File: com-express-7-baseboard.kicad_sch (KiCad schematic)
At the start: 0 parts

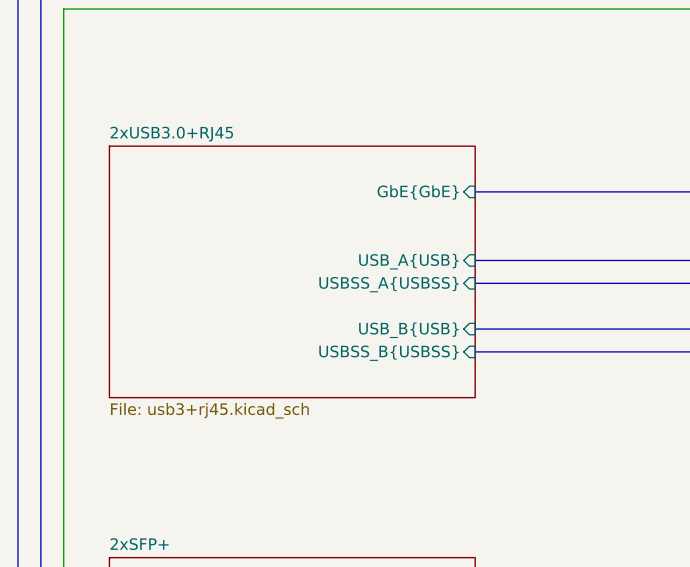
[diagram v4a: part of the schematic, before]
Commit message: [#57056] Connect USB 3.0 connectors on combo connector
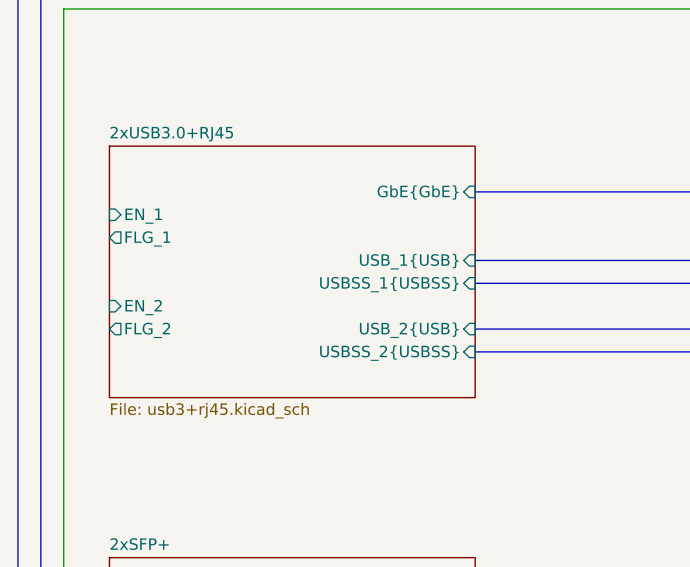
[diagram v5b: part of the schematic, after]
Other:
- sheet 2xUSB3.0+RJ45 ports: added EN_1, EN_2, FLG_1, FLG_2, USBSS_1{USBSS}, USBSS_2{USBSS}, USB_1{USB}, USB_2{USB}; removed USBSS_A{USBSS}, USBSS_B{USBSS}, USB_A{USB}, USB_B{USB}
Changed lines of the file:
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@@
       (effects (font (size 1.27 1.27)) (justify right))
     )
-    (pin "USBSS_A{USBSS}" input (at 137.16 73.66 0)
+    (pin "EN_1" input (at 96.52 66.04 180)
+      (effects (font (size 1.27 1.27)) (justify left))
+    )
+    (pin "FLG_1" output (at 96.52 68.58 180)
+      (effects (font (size 1.27 1.27)) (justify left))
+    )
+    (pin "USB_1{USB}" input (at 137.16 71.12 0)
       (effects (font (size 1.27 1.27)) (justify right))
     )
-    (pin "USBSS_B{USBSS}" input (at 137.16 81.28 0)
+    (pin "USBSS_1{USBSS}" input (at 137.16 73.66 0)
       (effects (font (size 1.27 1.27)) (justify right))
     )
-    (pin "USB_A{USB}" input (at 137.16 71.12 0)
+    (pin "USB_2{USB}" input (at 137.16 78.74 0)
       (effects (font (size 1.27 1.27)) (justify right))
     )
-    (pin "USB_B{USB}" input (at 137.16 78.74 0)
+    (pin "USBSS_2{USBSS}" input (at 137.16 81.28 0)
       (effects (font (size 1.27 1.27)) (justify right))
     )
+    (pin "EN_2" input (at 96.52 76.2 180)
+      (effects (font (size 1.27 1.27)) (justify left))
+    )
+    (pin "FLG_2" output (at 96.52 78.74 180)
+      (effects (font (size 1.27 1.27)) (justify left))
+    )
     (instances

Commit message: [#57056] Connect GbE
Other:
- sheet 2xUSB3.0+RJ45 ports: added ~{GBE0_ACT}, ~{GBE0_LINK_1000}, ~{GBE0_LINK_100}; removed none
- sheet Com Express 7 Interfaces ports: added ~{GBE0_ACT}, ~{GBE0_LINK_1000}, ~{GBE0_LINK_100}; removed none
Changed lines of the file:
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@@
     (stroke (width 0) (type default) (color 0 0 255 1))
   )
-  (bus (pts (xy 137.16 73.66) (xy 162.56 73.66))
+  (bus (pts (xy 137.16 81.28) (xy 162.56 81.28))
     (stroke (width 0) (type default) (color 0 255 255 1))
   )
@@
     (stroke (width 0) (type default) (color 255 0 0 1))
   )
+  (wire (pts (xy 137.16 73.66) (xy 162.56 73.66))
+    (stroke (width 0) (type default))
+  )
   (bus (pts (xy 96.52 152.4) (xy 86.36 152.4))
     (stroke (width 0) (type default))
@@
     (stroke (width 0) (type default))
   )
-  (bus (pts (xy 137.16 71.12) (xy 162.56 71.12))
+  (bus (pts (xy 137.16 78.74) (xy 162.56 78.74))
     (stroke (width 0) (type default) (color 0 0 255 1))
   )
@@
     (stroke (width 0) (type default))
   )
-  (bus (pts (xy 137.16 78.74) (xy 162.56 78.74))
+  (bus (pts (xy 137.16 86.36) (xy 162.56 86.36))
     (stroke (width 0) (type default) (color 0 0 255 1))
   )
@@
     (stroke (width 0) (type default))
   )
-  (bus (pts (xy 137.16 81.28) (xy 162.56 81.28))
+  (bus (pts (xy 137.16 88.9) (xy 162.56 88.9))
     (stroke (width 0) (type default) (color 0 255 255 1))
   )
@@
     (stroke (width 0) (type default))
   )
+  (wire (pts (xy 137.16 68.58) (xy 162.56 68.58))
+    (stroke (width 0) (type default))
+  )
   (bus (pts (xy 248.92 180.34) (xy 259.08 180.34))
     (stroke (width 0) (type default) (color 255 153 0 1))
@@
     (stroke (width 0) (type default))
   )
+  (wire (pts (xy 137.16 71.12) (xy 162.56 71.12))
+    (stroke (width 0) (type default))
+  )
   (wire (pts (xy 325.12 66.04) (xy 325.12 35.56))
     (stroke (width 0) (type default))
@@
       (effects (font (size 1.27 1.27)) (justify right))
     )
-    (pin "USB3{USB}" output (at 162.56 78.74 180)
-      (effects (font (size 1.27 1.27)) (justify left))
-    )
-    (pin "USB2{USB}" output (at 162.56 71.12 180)
+    (pin "USB3{USB}" output (at 162.56 86.36 180)
+      (effects (font (size 1.27 1.27)) (justify left))
+    )
+    (pin "USB2{USB}" output (at 162.56 78.74 180)
       (effects (font (size 1.27 1.27)) (justify left))
     )
@@
       (effects (font (size 1.27 1.27)) (justify right))
     )
-    (pin "USBSS3{USBSS}" output (at 162.56 81.28 180)
-      (effects (font (size 1.27 1.27)) (justify left))
-    )
-    (pin "USBSS2{USBSS}" output (at 162.56 73.66 180)
+    (pin "USBSS3{USBSS}" output (at 162.56 88.9 180)
+      (effects (font (size 1.27 1.27)) (justify left))
+    )
+    (pin "USBSS2{USBSS}" output (at 162.56 81.28 180)
       (effects (font (size 1.27 1.27)) (justify left))
     )
@@
       (effects (font (size 1.27 1.27)) (justify right))
     )
+    (pin "~{GBE0_ACT}" output (at 162.56 73.66 180)
+      (effects (font (size 1.27 1.27)) (justify left))
+    )
+    (pin "~{GBE0_LINK_1000}" output (at 162.56 68.58 180)
+      (effects (font (size 1.27 1.27)) (justify left))
+    )
+    (pin "~{GBE0_LINK_100}" output (at 162.56 71.12 180)
+      (effects (font (size 1.27 1.27)) (justify left))
+    )
     (instances
       (project "com-express-7-baseboard"
@@
     )
   )
-  (sheet (at 96.52 58.42) (size 40.64 27.94) (fields_autoplaced)
+  (sheet (at 96.52 58.42) (size 40.64 33.02) (fields_autoplaced)
     (stroke (width 0.1524) (type solid))
     (fill (color 0 0 0 0.0000))
@@
       (effects (font (size 1.27 1.27)) (justify left bottom))
     )
-    (property "Sheetfile" "usb3+rj45.kicad_sch" (at 96.52 86.9446 0)
+    (property "Sheetfile" "usb3+rj45.kicad_sch" (at 96.52 92.0246 0)
       (effects (font (size 1.27 1.27)) (justify left top))
     )
@@
       (effects (font (size 1.27 1.27)) (justify left))
     )
-    (pin "USB_1{USB}" input (at 137.16 71.12 0)
-      (effects (font (size 1.27 1.27)) (justify right))
-    )
-    (pin "USBSS_1{USBSS}" input (at 137.16 73.66 0)
-      (effects (font (size 1.27 1.27)) (justify right))
-    )
-    (pin "USB_2{USB}" input (at 137.16 78.74 0)
-      (effects (font (size 1.27 1.27)) (justify right))
-    )
-    (pin "USBSS_2{USBSS}" input (at 137.16 81.28 0)
+    (pin "USB_1{USB}" input (at 137.16 78.74 0)
+      (effects (font (size 1.27 1.27)) (justify right))
+    )
+    (pin "USBSS_1{USBSS}" input (at 137.16 81.28 0)
+      (effects (font (size 1.27 1.27)) (justify right))
+    )
+    (pin "USB_2{USB}" input (at 137.16 86.36 0)
+      (effects (font (size 1.27 1.27)) (justify right))
+    )
+    (pin "USBSS_2{USBSS}" input (at 137.16 88.9 0)
       (effects (font (size 1.27 1.27)) (justify right))
     )
@@
       (effects (font (size 1.27 1.27)) (justify left))
     )
-    (instances
+    (pin "~{GBE0_LINK_1000}" input (at 137.16 68.58 0)
+      (effects (font (size 1.27 1.27)) (justify right))
+    )
+    (pin "~{GBE0_ACT}" input (at 137.16 73.66 0)
+      (effects (font (size 1.27 1.27)) (justify right))
+    )
+    (pin "~{GBE0_LINK_100}" input (at 137.16 71.12 0)
+      (effects (font (size 1.27 1.27)) (justify right))
+    )
+    (instances

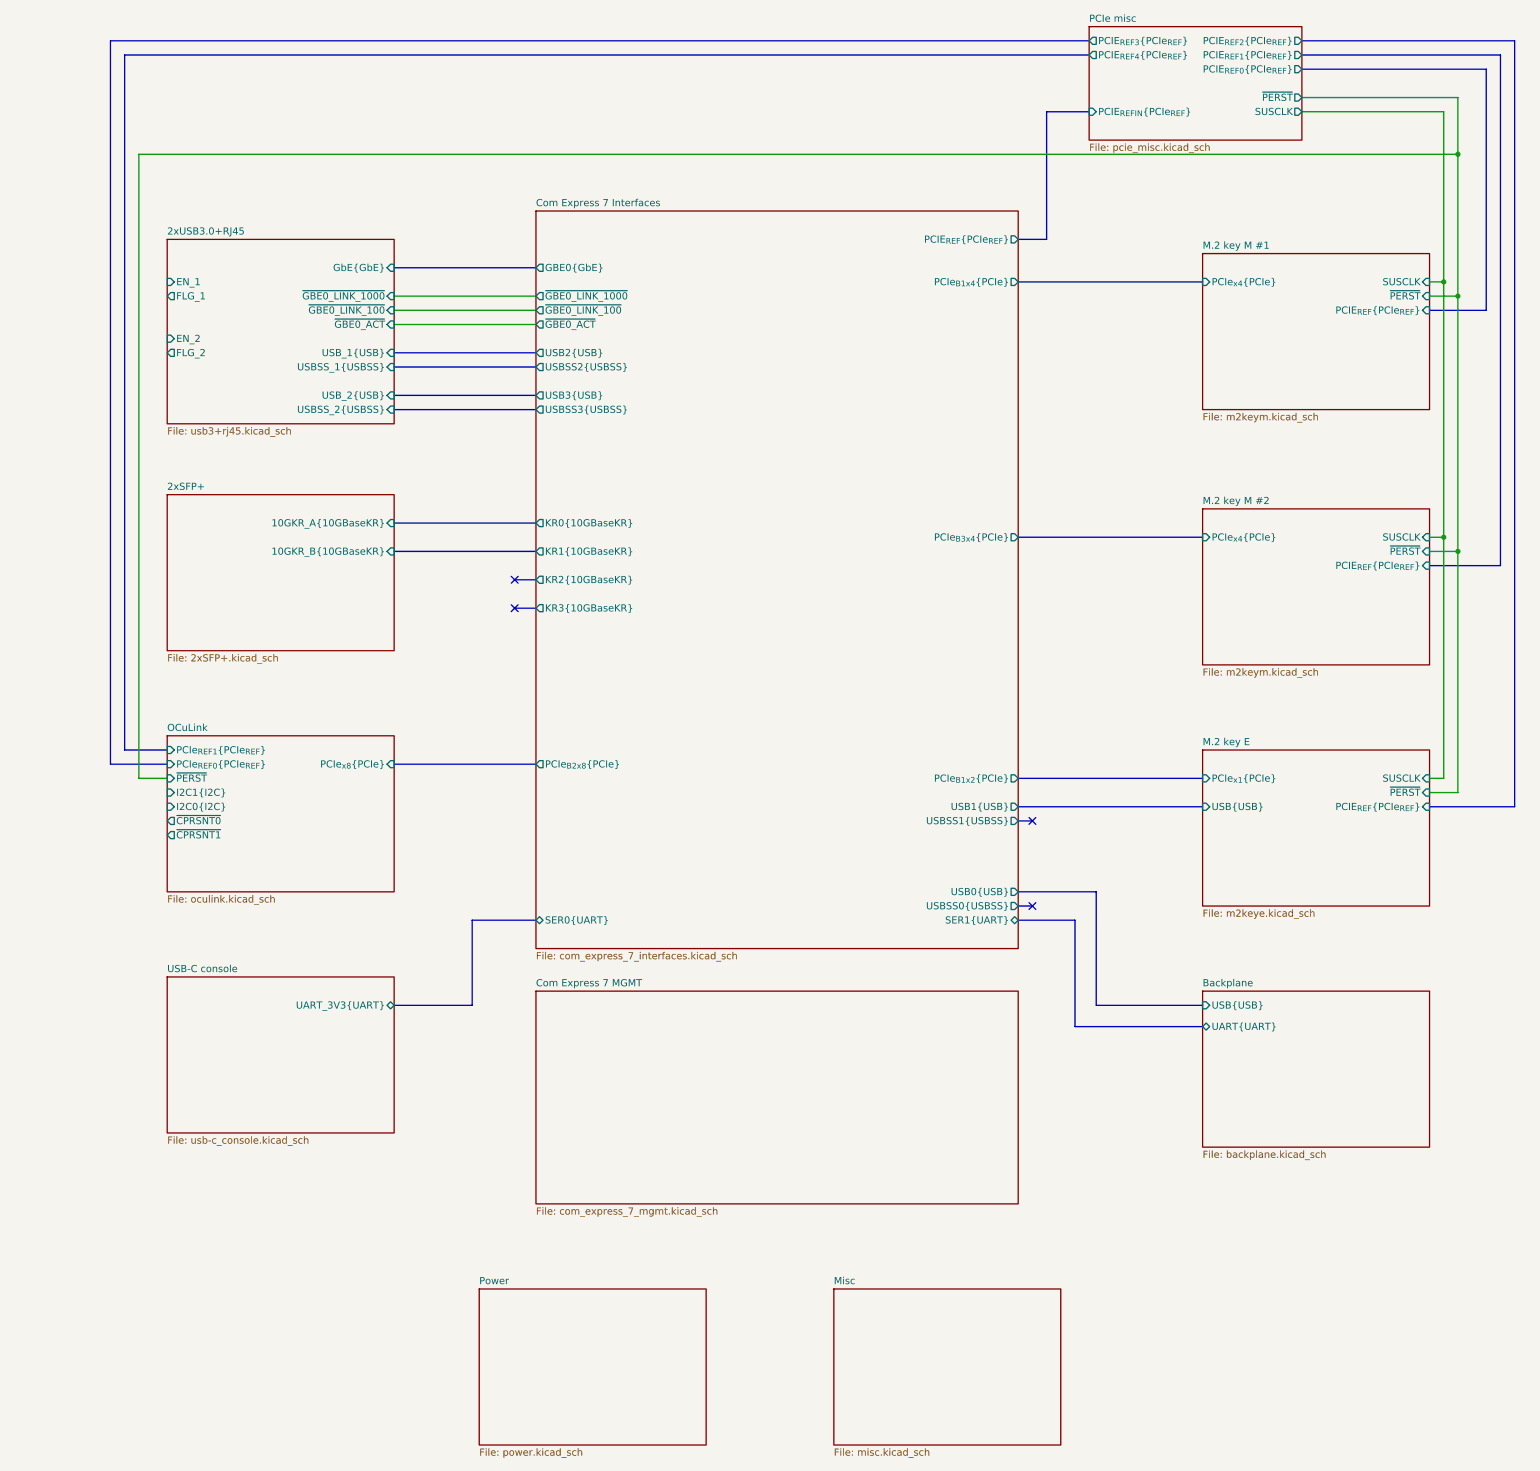
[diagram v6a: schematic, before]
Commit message: [#57056] Update top sheet, update sheet's dates
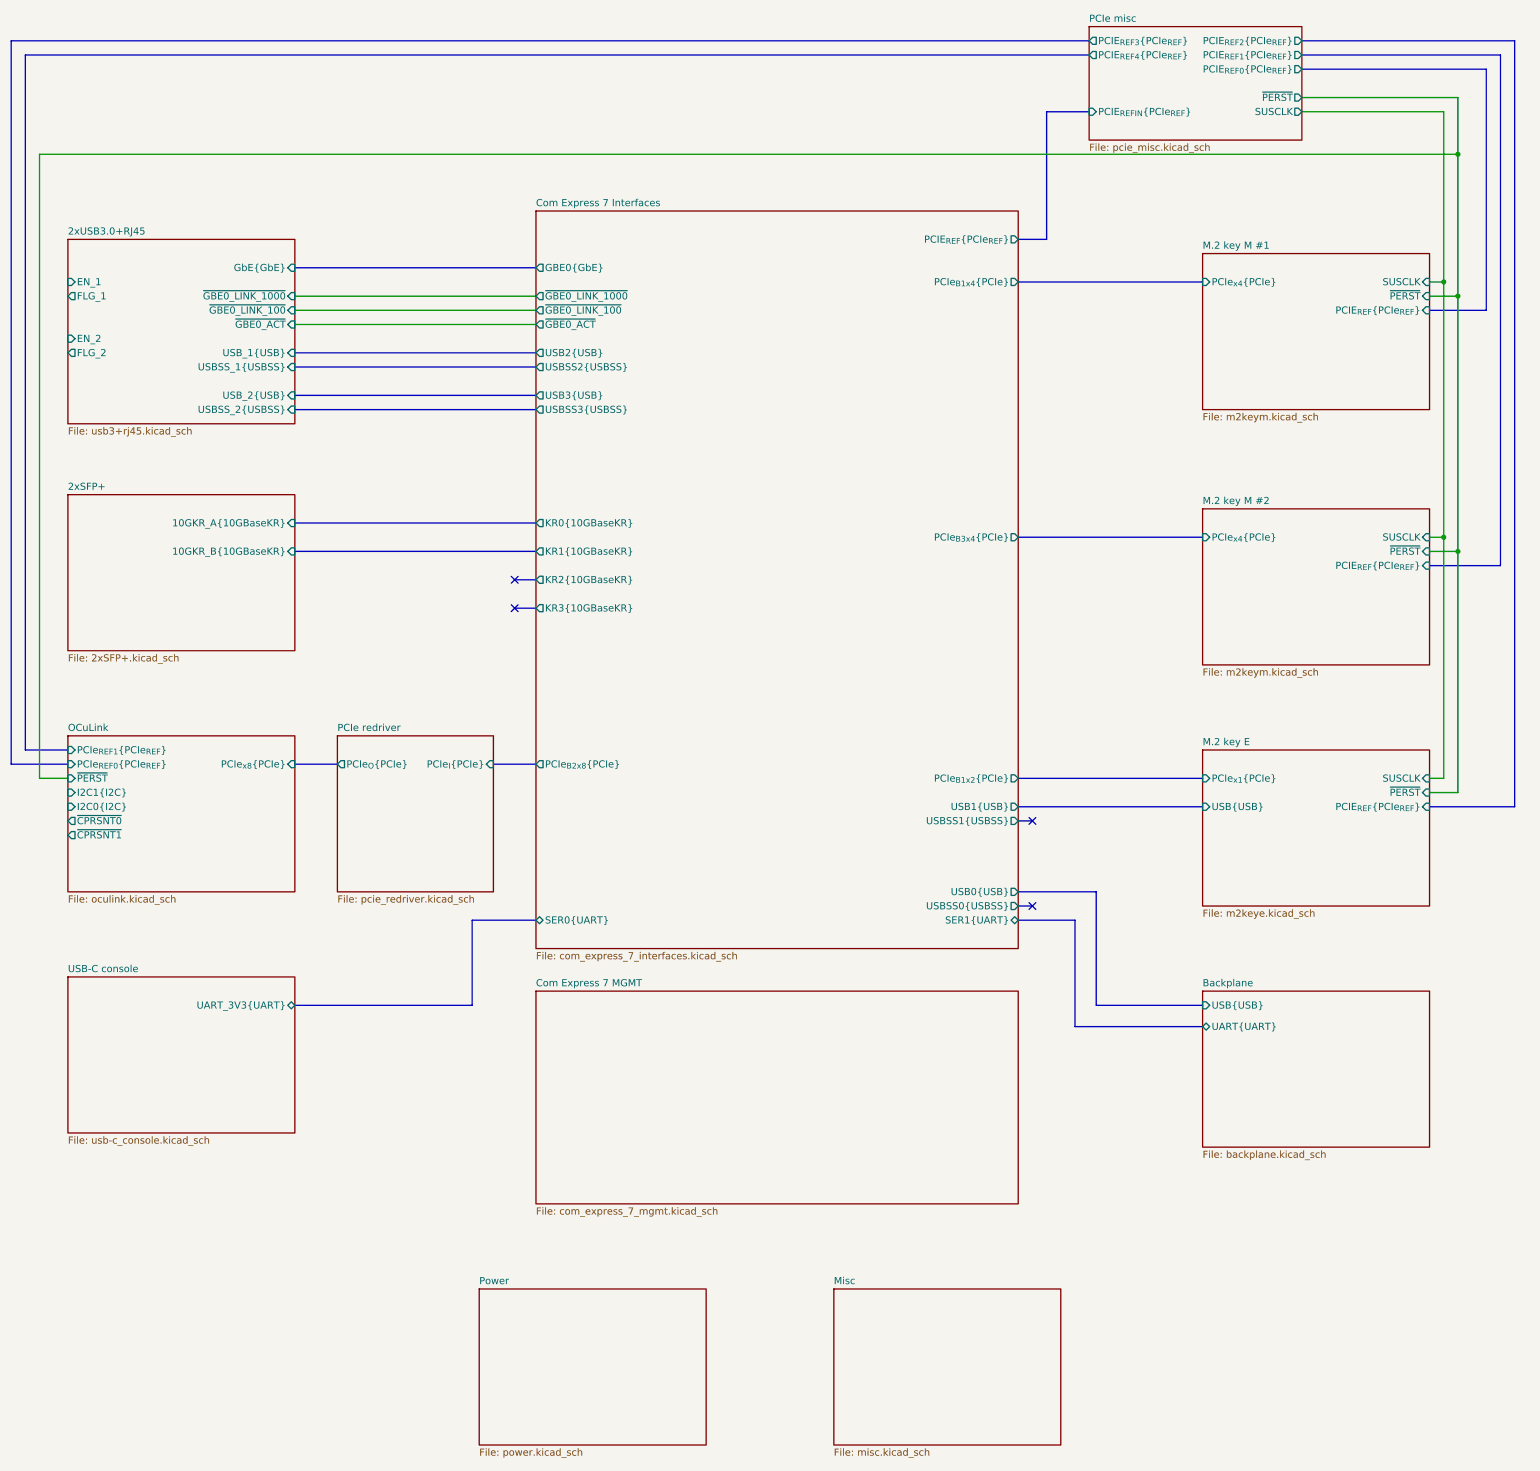
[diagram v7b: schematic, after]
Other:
- added sheet PCIe redriver (pcie_redriver.kicad_sch)

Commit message: [#57056] Update PCIe lane assignment, drop 2nd OCuLink
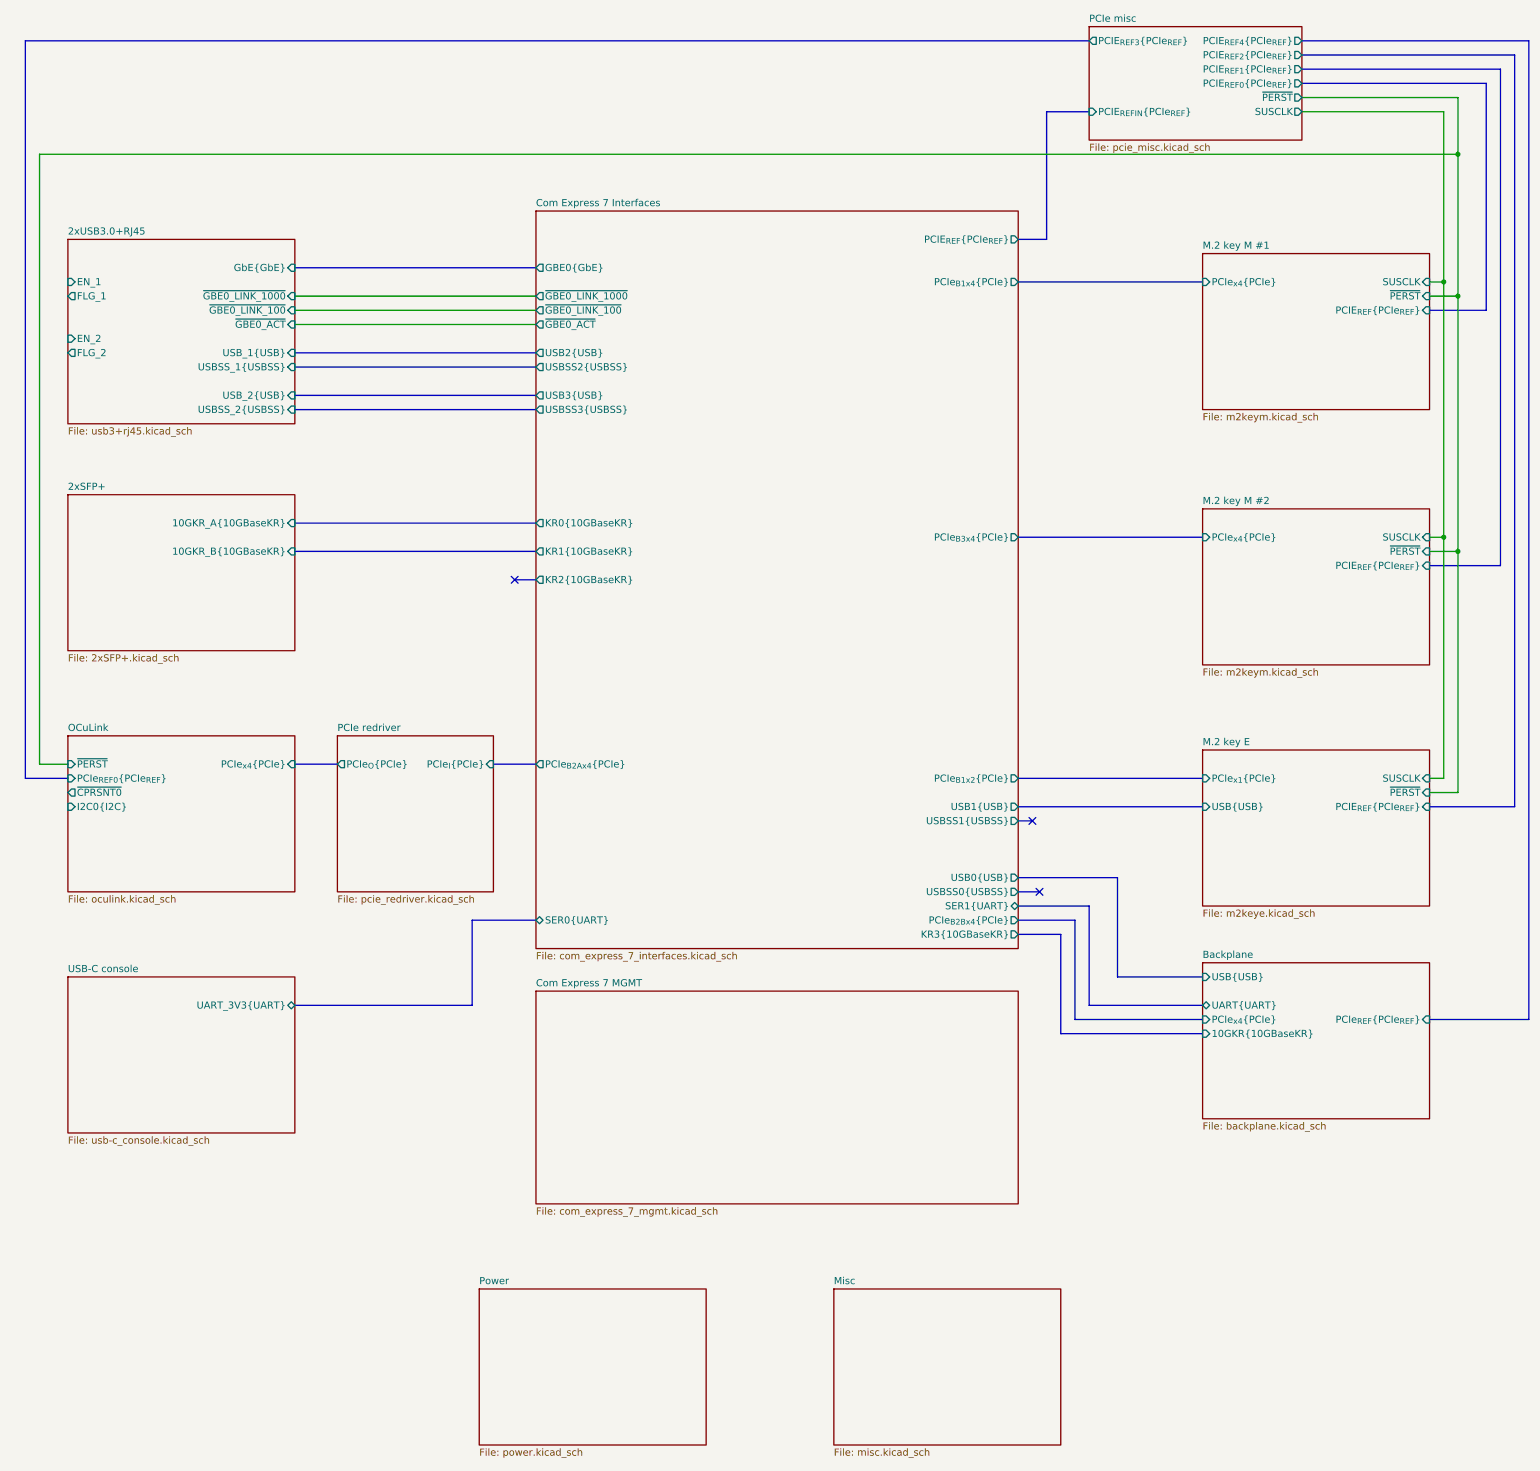
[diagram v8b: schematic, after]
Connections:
- no-connect marks 4 -> 3
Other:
- sheet Backplane ports: added 10GKR{10GBaseKR}, PCIe_{REF}{PCIe_{REF}}, PCIe_{x4}{PCIe}; removed none
- sheet Com Express 7 Interfaces ports: added PCIe_{B2Ax4}{PCIe}, PCIe_{B2Bx4}{PCIe}; removed PCIe_{B2x8}{PCIe}
- sheet OCuLink ports: added PCIe_{x4}{PCIe}; removed I2C1{I2C}, PCIe_{REF1}{PCIe_{REF}}, PCIe_{x8}{PCIe}, ~{CPRSNT1}
